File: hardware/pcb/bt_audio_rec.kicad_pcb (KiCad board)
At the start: 2 copper layers, 54 x 82 mm, 63 parts, among them IC1 RN52-I_RM116, IC2 VCNL4200, J1 OutL, J13 Power, J14 PROX Socket, J15 PROX Header, J2 Conn_01x31, J3 RN52 factory reset, J4 ERM, J5 OutR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

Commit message: Fix GPIO4 tied low and backwards MOSFET error
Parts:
- removed ?: , BOB_Dukio:dukio-20mm
- removed R9: 10k, Resistor_SMD:R_0603_1608Metric
- C12: value 2.2uF -> 4.7uF
- J3: footprint Connector_PinHeader_2.54mm:PinHeader_1x02_P2.54mm_Horizontal -> Connector_PinHeader_2.54mm:PinHeader_1x03_P2.54mm_Horizontal
- moved J3 3.28 mm to (219.2, 97.0)
- moved Q4 0.14 mm to (252.1, 147.4), turned to 270 degrees
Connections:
- Q4 pad 2: LED+ -> PROX_3.3V
- Q4 pad 3: PROX_3.3V -> LED+
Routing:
- net 3.3V: track 146.4 -> 143.5 mm
- net RN52_RST: track 36.5 -> 39.3 mm
- net LED_CATHODE: track 5.77 -> 3.92 mm, vias 2 -> 0
- net LED+: track 5.16 -> 5.94 mm
- net PROX_3.3V: track 37.5 -> 37.9 mm, vias 3 -> 4
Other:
- board text added: "Bluetooth Media Player Revision 1b"
- board text added: "GPIO4"
- board text removed: "Bluetooth Media Player Revision 1a"

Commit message: Add duk.io logo
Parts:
- added ?: , BOB_Dukio:dukio-20mm, B.Cu at (243.0, 92.3)

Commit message: Change LED resistor
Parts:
- removed ?: , BOB_Dukio:dukio-20mm
- J2: value Conn_01x31 -> AYF333135
- R13: value 3.6R -> 1.8R
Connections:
- U1 pad 10: Net-(U1-Pad10) -> AUDIO_GROUND
- U1 pad 14: Net-(U1-Pad14) -> AUDIO_GROUND
- U1 pad 29: Net-(U1-Pad29) -> AUDIO_GROUND
- U1 pad 3: Net-(U1-Pad3) -> AUDIO_GROUND
- U1 pad 38: Net-(U1-Pad38) -> AUDIO_GROUND
- U1 pad 4: Net-(U1-Pad4) -> AUDIO_GROUND
- U1 pad 41: Net-(U1-Pad41) -> AUDIO_GROUND
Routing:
- net Net-(U1-Pad10): track 0.73 -> 0.00 mm
- net AUDIO_GROUND: track 2.45 -> 3.19 mm

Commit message: Add FPC pin number label
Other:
- board text added: "1"

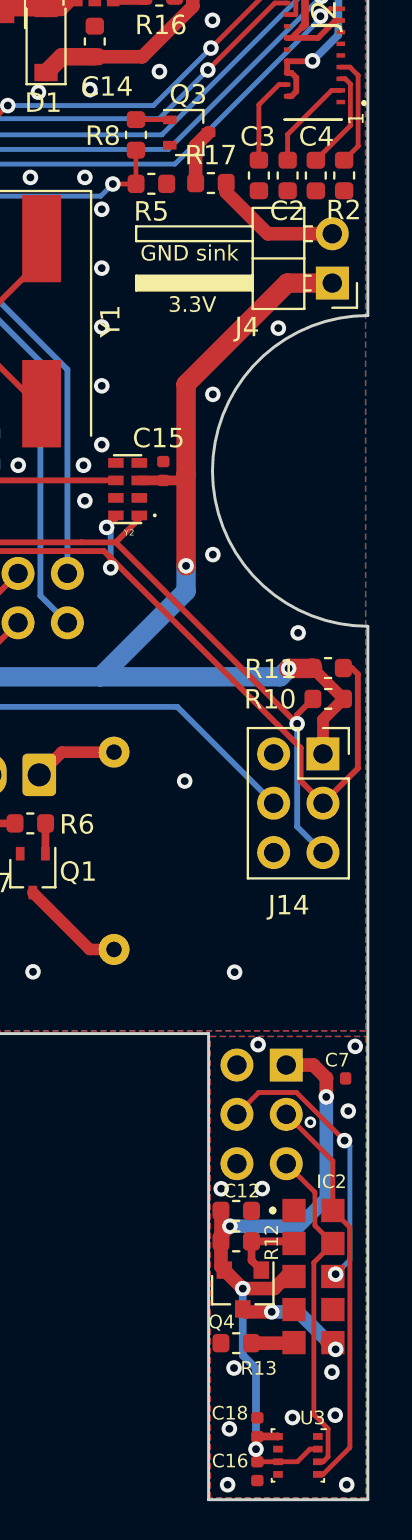
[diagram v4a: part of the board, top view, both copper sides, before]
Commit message: Add decoupling cap to proximity LED
See https://www.duk.io/blog/electronics-projects/bt-player/bluetooth-audio-player-firmware
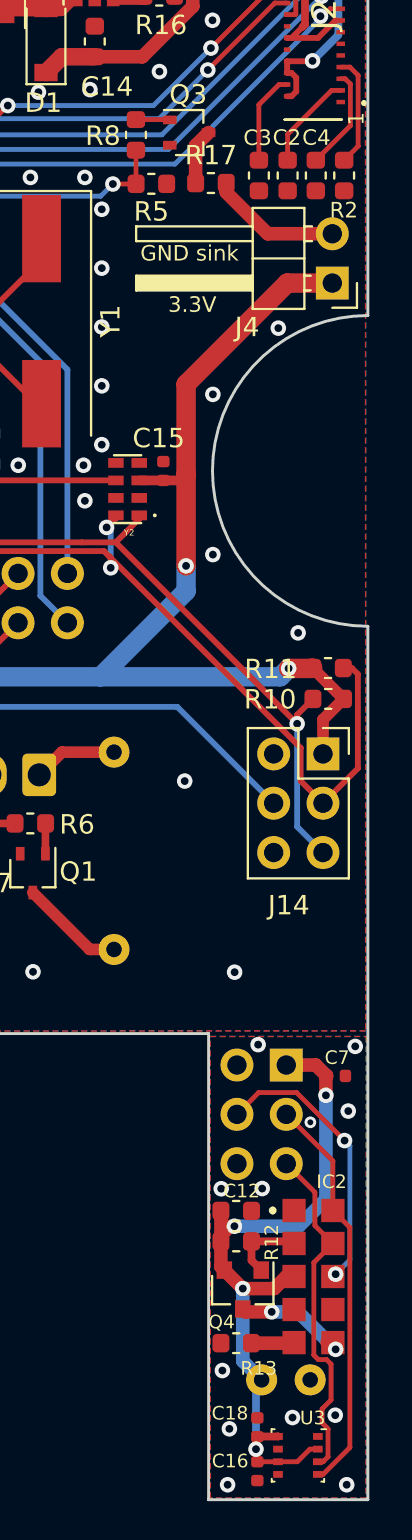
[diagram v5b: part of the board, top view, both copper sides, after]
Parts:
- added C19: 680uF, Capacitor_THT:C_Radial_D6.3mm_H7.0mm_P2.50mm, B.Cu at (253.0, 152.1)
- moved C7 0.13 mm to (256.9, 136.4)
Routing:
- net PROX_I2C_SDA: track 17.4 -> 18.1 mm
- net PROX_GND: vias 13 -> 12
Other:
- board text added: "Bluetooth Media Player Revision 1c"
- board text removed: "Bluetooth Media Player Revision 1b"

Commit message: Migrate to KiCad 7
Update schematic/pcb and rescue symbols as required
Move custom library to a project specific submodule
Fix missing duk.io logo
Update gitignore
Remove old files
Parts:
- added ?: , .MyCustom_dukio_logos:dukio-20mm, B.Cu at (242.4, 92.0)
- IC1: footprint BOB_General:Bluetooth_module_Microchip_RN52 -> .MyCustom_general:Bluetooth_module_Microchip_RN52
- IC2: footprint BOB_General:Proximity_Sensor_Vishay_VCNL4200 -> .MyCustom_general:Proximity_Sensor_Vishay_VCNL4200
- J2: footprint BOB_General:FPC_Socket_0.3_31_Panasonic_AYF333135 -> .MyCustom_general:FPC_Socket_0.3_31_Panasonic_AYF333135
- L1: footprint BOB_General:Inductor_L_TDK_VLCF4024 -> .MyCustom_general:Inductor_L_TDK_VLCF4024
- Y2: footprint BOB_General:RTC_Microcrystal_RV-8803-C7-TA-QC -> .MyCustom_general:RTC_Microcrystal_RV-8803-C7-TA-QC
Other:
- net class Default removed
